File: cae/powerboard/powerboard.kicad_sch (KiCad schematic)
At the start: 74 parts

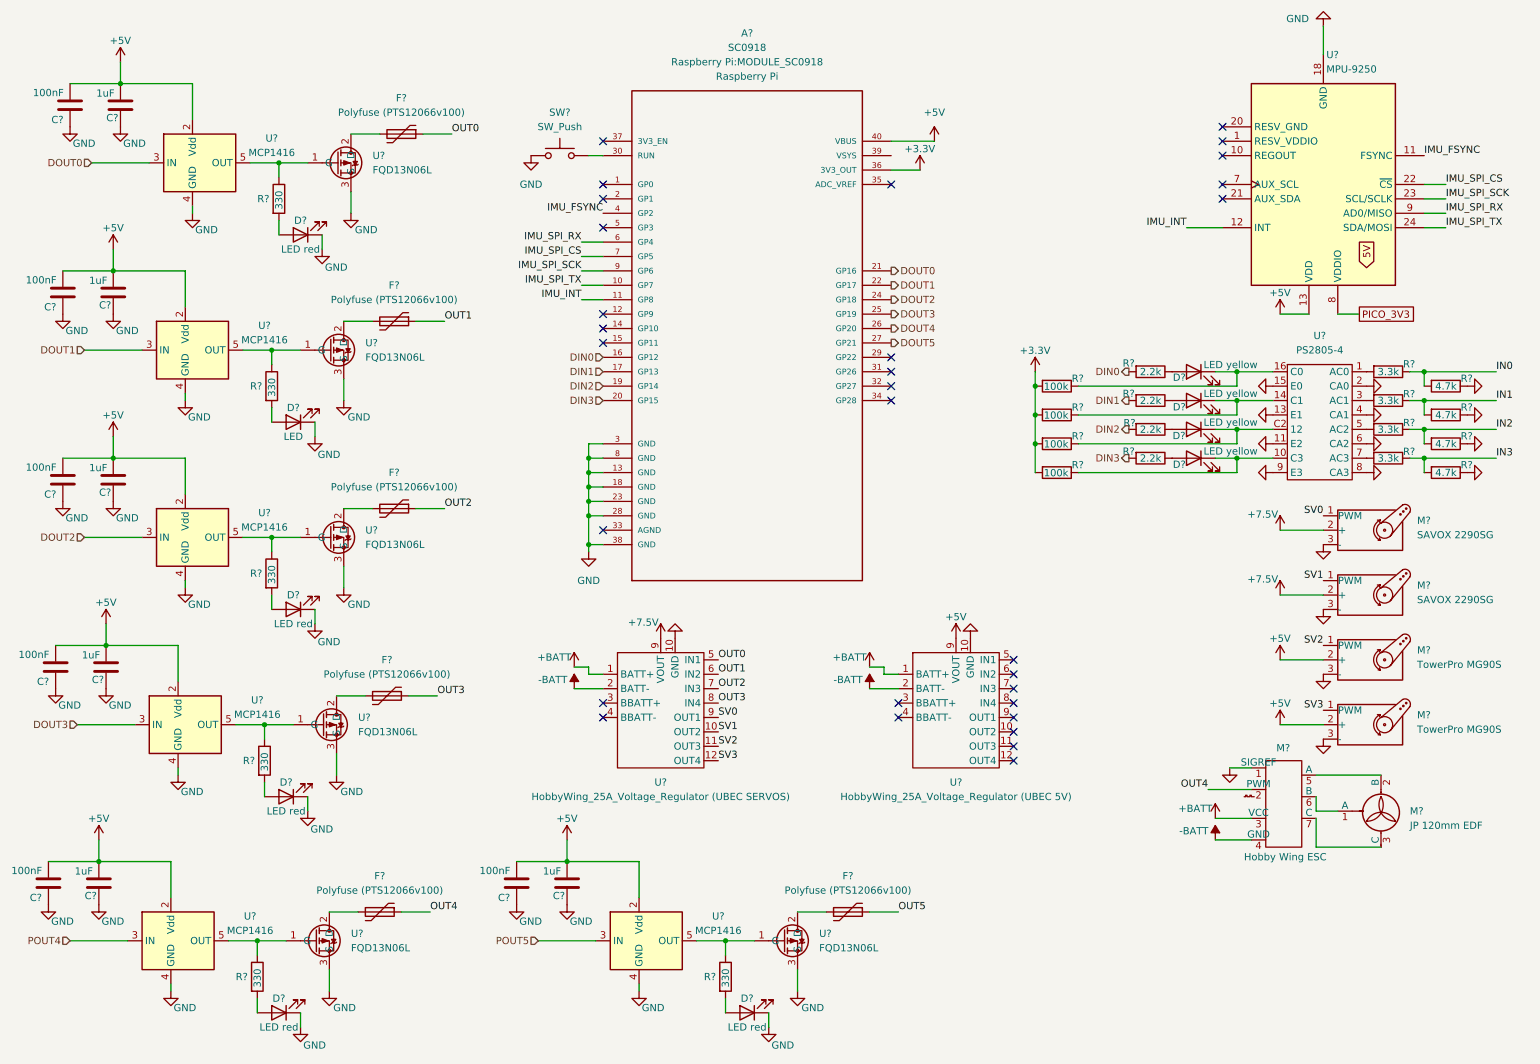
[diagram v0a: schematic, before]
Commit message: begin editing first pictures
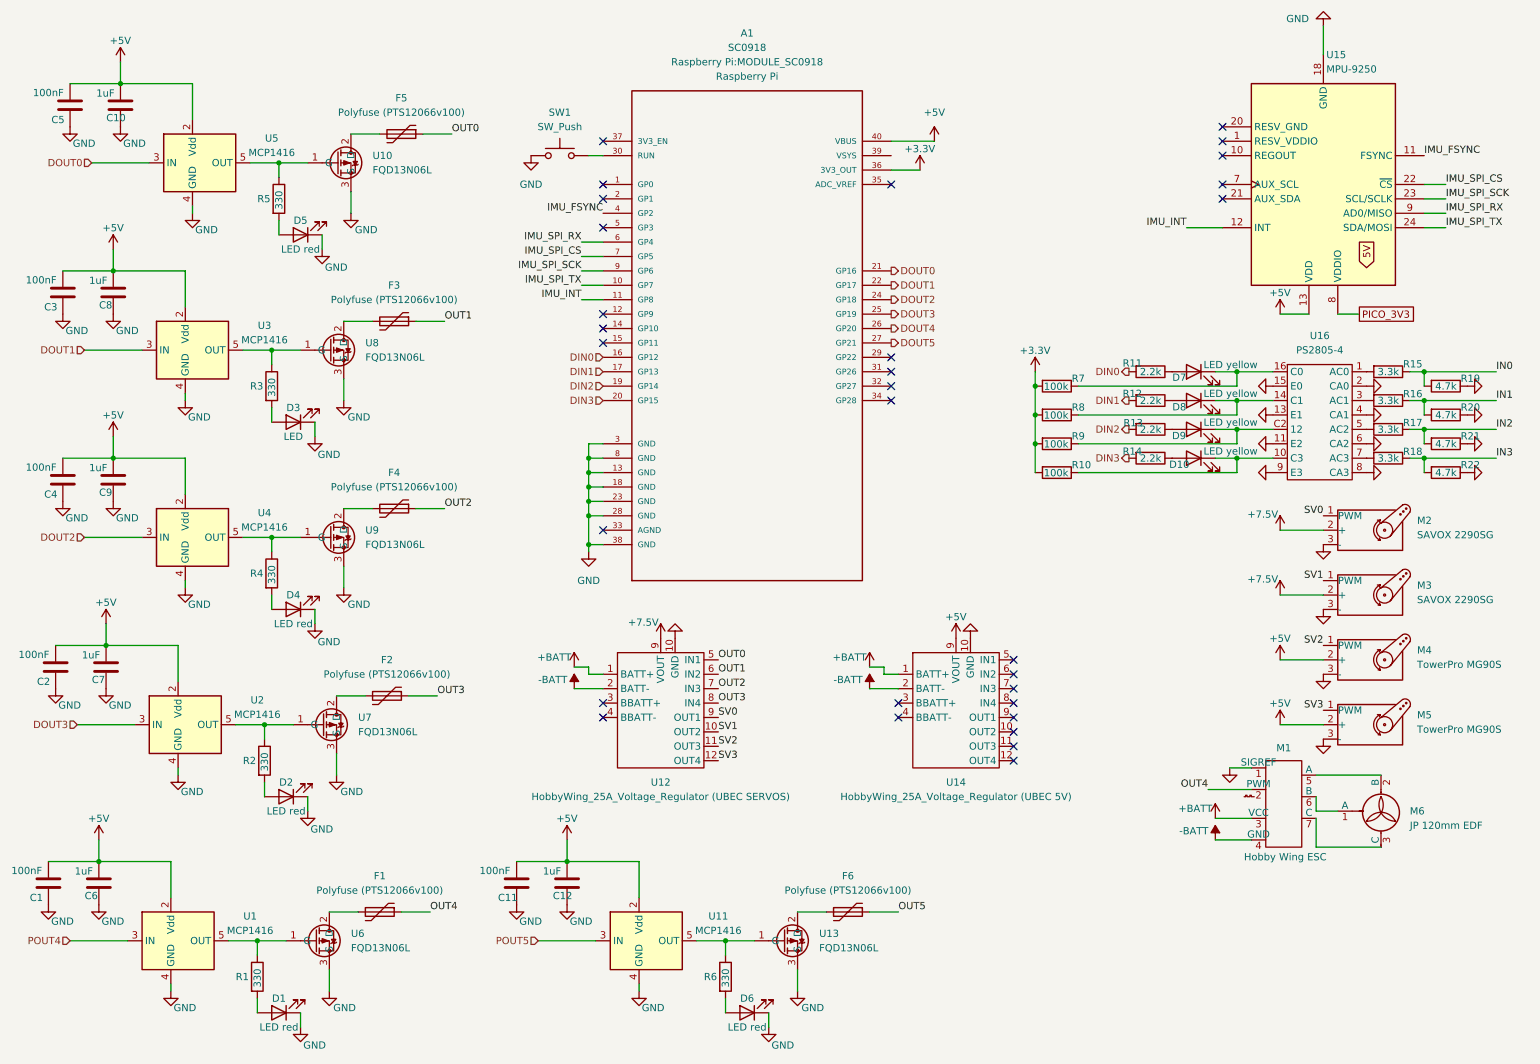
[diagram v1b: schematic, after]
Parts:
- R1, R2, R3, R5, R6: renamed from R?; footprint (none) -> Resistor_SMD:R_0201_0603Metric
- U10, U13, U6, U7, U8, U9: renamed from U?; footprint (none) -> Package_TO_SOT_SMD:SOT-223
- gave numbers to parts that had none: 63
